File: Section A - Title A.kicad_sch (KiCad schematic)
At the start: 0 parts

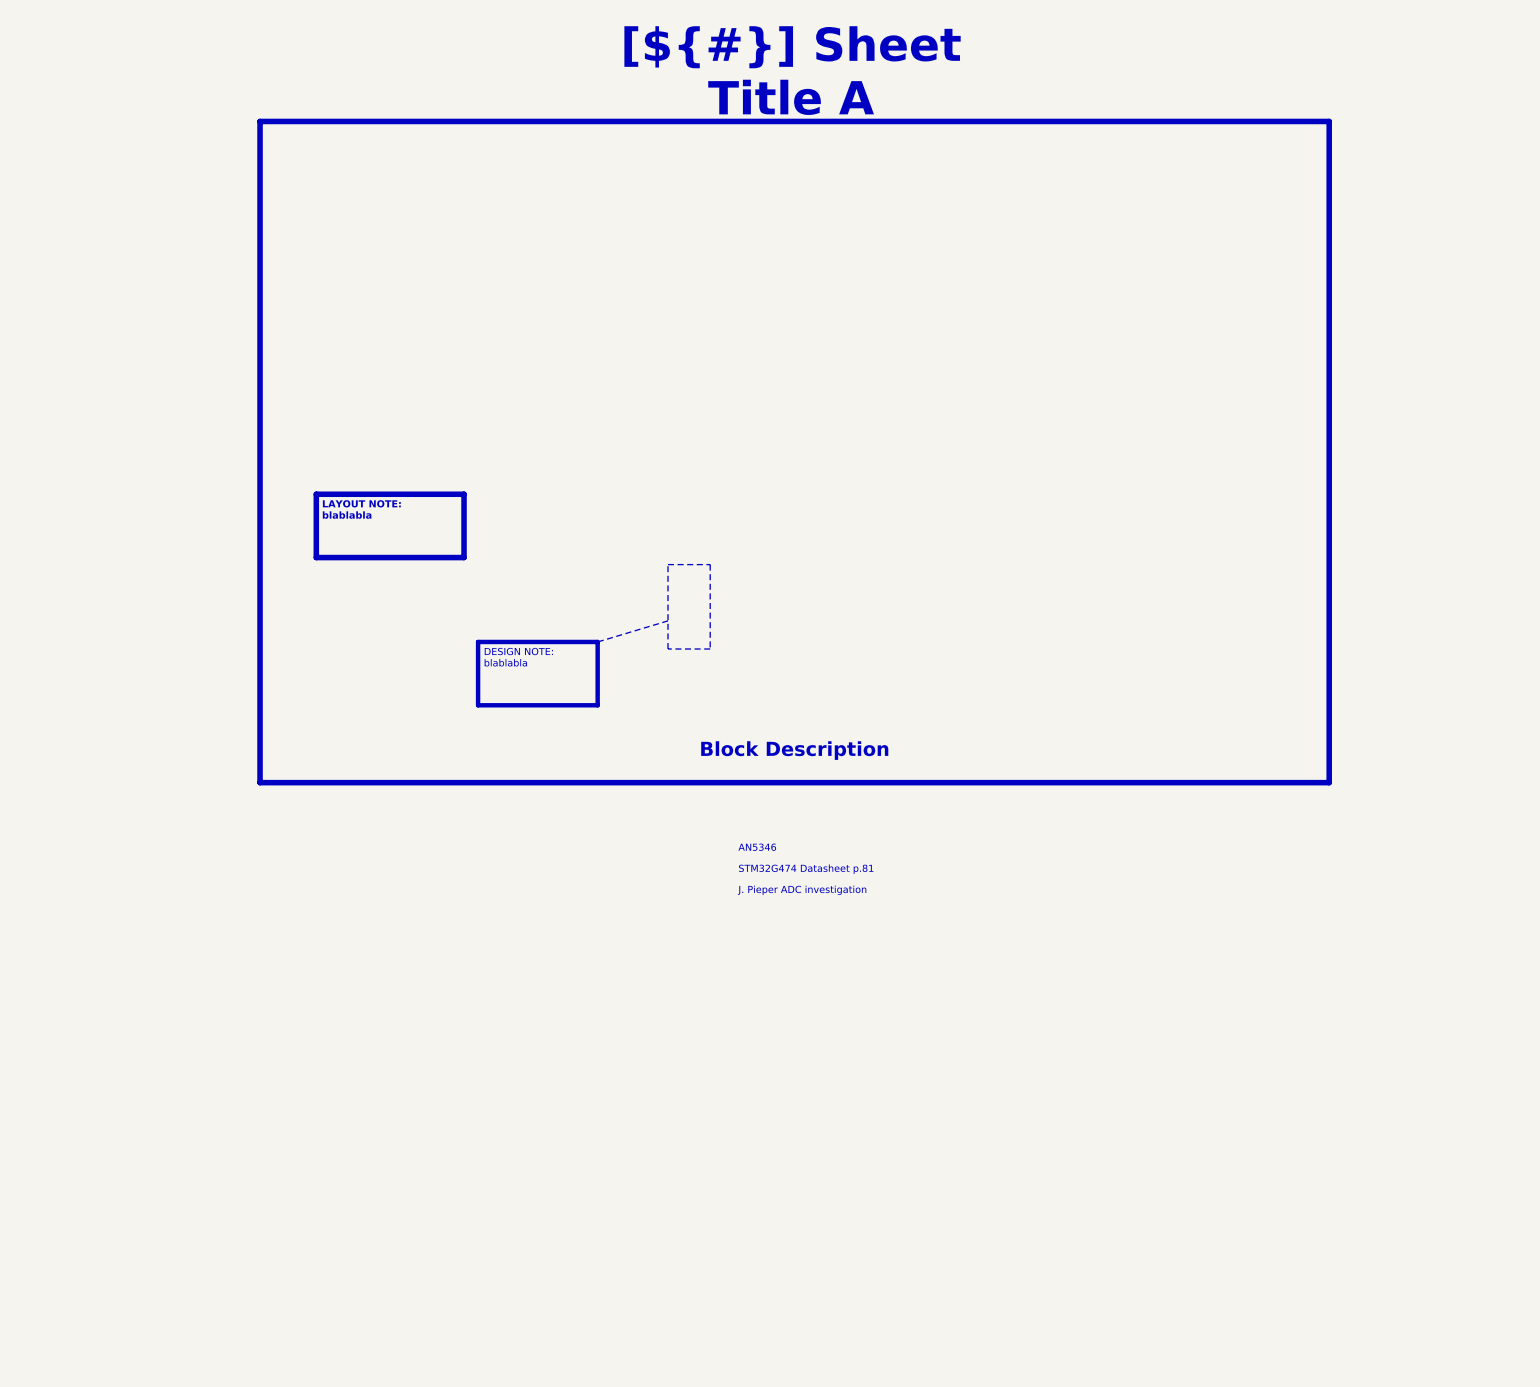
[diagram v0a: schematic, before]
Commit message: added PHY & RJ45 plug
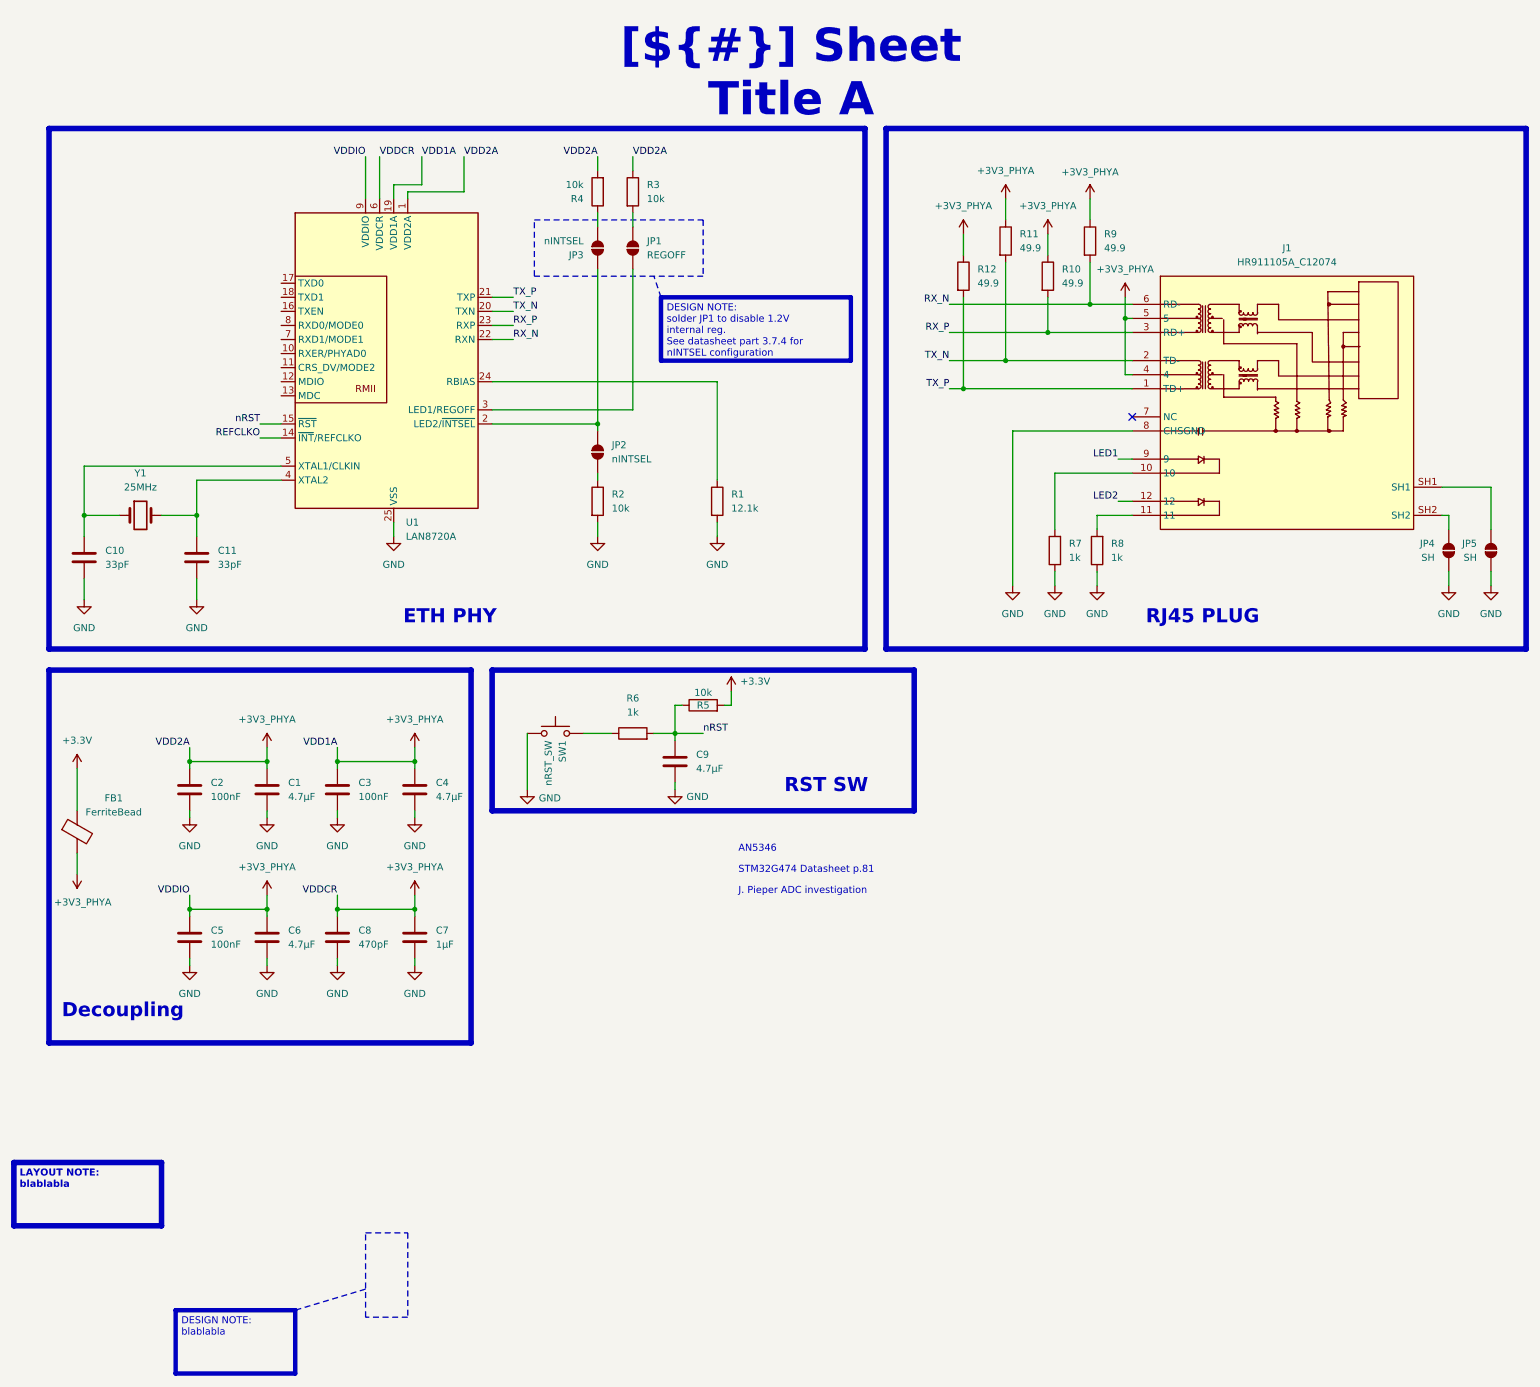
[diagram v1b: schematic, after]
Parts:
- added C1, C4, C6, C9: 4.7µF, Capacitor_SMD:C_0603_1608Metric_Pad1.08x0.95mm_HandSolder, symbol Device:C
- added C10, C11: 33pF, Capacitor_SMD:C_0603_1608Metric_Pad1.08x0.95mm_HandSolder, symbol Device:C
- added C2, C3, C5: 100nF, Capacitor_SMD:C_0603_1608Metric_Pad1.08x0.95mm_HandSolder, symbol Device:C
- added C7: 1µF, Capacitor_SMD:C_0603_1608Metric_Pad1.08x0.95mm_HandSolder, symbol Device:C
- added C8: 470pF, Capacitor_SMD:C_0603_1608Metric_Pad1.08x0.95mm_HandSolder, symbol Device:C
- added FB1: FerriteBead, symbol Device:FerriteBead
- added J1: HR911105A_C12074, 0_connector:RJ45-TH_HR911105A, symbol 0_connector:HR911105A_C12074
- added JP1: REGOFF, Jumper:SolderJumper-2_P1.3mm_Open_RoundedPad1.0x1.5mm, symbol Jumper:SolderJumper_2_Open
- added JP2: nINTSEL, Jumper:SolderJumper-2_P1.3mm_Bridged_RoundedPad1.0x1.5mm, symbol Jumper:SolderJumper_2_Open
- added JP3: nINTSEL, Jumper:SolderJumper-2_P1.3mm_Open_RoundedPad1.0x1.5mm, symbol Jumper:SolderJumper_2_Open
- added JP4, JP5: SH, Jumper:SolderJumper-2_P1.3mm_Bridged_RoundedPad1.0x1.5mm, symbol Jumper:SolderJumper_2_Open
- added R1: 12.1k, Resistor_SMD:R_0603_1608Metric_Pad0.98x0.95mm_HandSolder, symbol Device:R
- added R10, R11, R12, R9: 49.9, Resistor_SMD:R_0603_1608Metric_Pad0.98x0.95mm_HandSolder, symbol Device:R
- added R2, R3, R4, R5: 10k, Resistor_SMD:R_0603_1608Metric_Pad0.98x0.95mm_HandSolder, symbol Device:R
- added R6, R7, R8: 1k, Resistor_SMD:R_0603_1608Metric_Pad0.98x0.95mm_HandSolder, symbol Device:R
- added SW1: nRST_SW, symbol Switch:SW_Push
- added U1: LAN8720A, Package_DFN_QFN:VQFN-24-1EP_4x4mm_P0.5mm_EP2.5x2.5mm_ThermalVias, symbol Interface_Ethernet:LAN8720A
- added Y1: 25MHz, symbol Device:Crystal
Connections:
- new net: JP1.1 (A), U1.3 (LED1/REGOFF)
- new net: JP1.2 (B), R3.2
- new net: JP3.1 (A), R4.1
- new net: R6.1, SW1.2
- new net: R1.1, U1.24 (RBIAS)
- new net: JP2.2 (B), JP3.2 (B), U1.2 (LED2/~{INTSEL})
- new net: C11.1, U1.4 (XTAL2), Y1.2
- new net: C10.1, U1.5 (XTAL1/CLKIN), Y1.1
- new net: JP2.1 (A), R2.1
- new net: J1.10, R7.2
- new net: J1.11, R8.2
- new net: J1.SH1, JP5.2 (B)
- new net: J1.SH2, JP4.2 (B)
- new net +3.3V: FB1.1, R5.2
- new net +3V3_PHYA: C1.1, C2.1, C3.1, C4.1, C5.1, C6.1, C7.1, C8.1, FB1.2, J1.4, J1.5, R10.1, R11.1, R12.1, R3.1, R4.2, R9.1, U1.1 (VDD2A), U1.19 (VDD1A), U1.6 (VDDCR), U1.9 (VDDIO)
- new net GND: C1.2, C10.2, C11.2, C2.2, C3.2, C4.2, C5.2, C6.2, C7.2, C8.2, C9.2, J1.8 (CHSGND), JP4.1 (A), JP5.1 (A), R1.2, R2.2, R7.1, R8.1, SW1.1, U1.25 (VSS)
- new net LED1: J1.9
- new net LED2: J1.12
- new net REFCLKO: U1.14 (~{INT}/REFCLKO)
- new net RX_N: J1.6 (RD-), R9.2, U1.22 (RXN)
- new net RX_P: J1.3 (RD+), R10.2, U1.23 (RXP)
- new net TX_N: J1.2 (TD-), R11.2, U1.20 (TXN)
- new net TX_P: J1.1 (TD+), R12.2, U1.21 (TXP)
- new net nRST: C9.1, R5.1, R6.2, U1.15 (~{RST})
- no-connect marks 0 -> 1
